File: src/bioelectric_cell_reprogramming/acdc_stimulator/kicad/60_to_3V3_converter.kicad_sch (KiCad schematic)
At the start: 7 parts, among them IC6 LTC3637IMSE#PBF

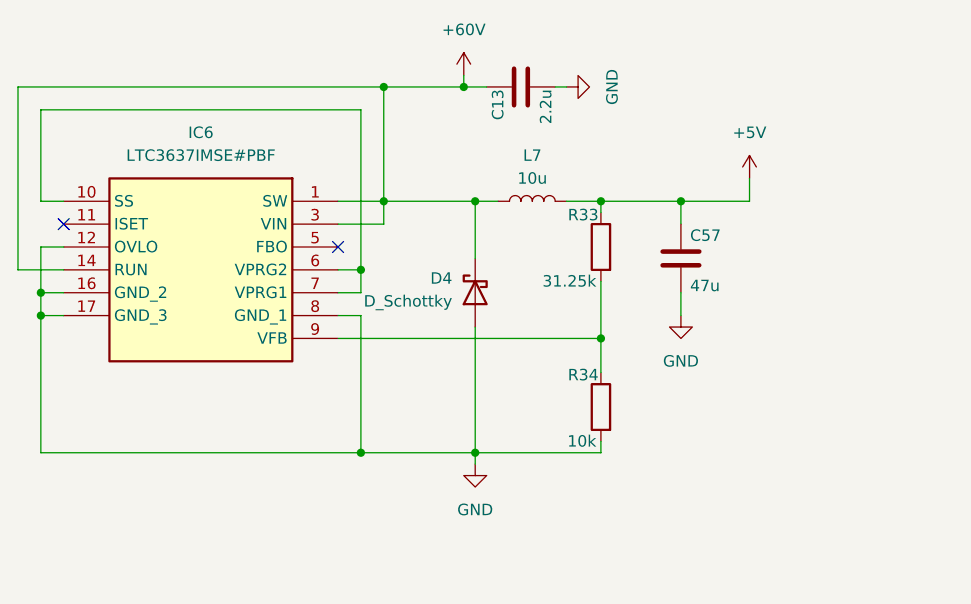
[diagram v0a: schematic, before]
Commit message: CI: footprint assignment done
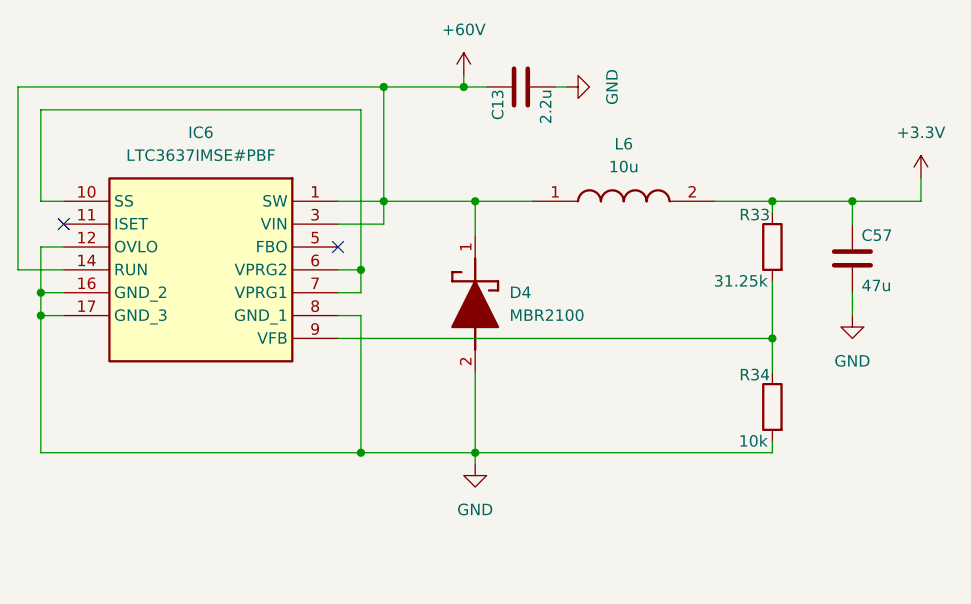
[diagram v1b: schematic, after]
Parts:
- removed D4: D_Schottky, symbol Device:D_Schottky
- removed L7: 10u, symbol Device:L
- added D4: MBR2100, MBR2100:DIOAD1910W86L670D310, symbol MBR2100:MBR2100
- added L6: 10u, SRP1270-100M:INDPM137137X700N, symbol SRP1270-100M:SRP1270-100M
- C13: footprint (none) -> Capacitor_SMD:C_0603_1608Metric
- C57: footprint (none) -> Capacitor_SMD:C_0805_2012Metric
- IC6: footprint LTC3637IMSEPBF -> LTC3637IMSE#PBF:LTC3637IMSEPBF
- R33, R34: footprint (none) -> Resistor_SMD:R_0402_1005Metric
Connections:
- net +60V: now also D4.1 (K), L6.1
- net GND: now also D4.2 (A)
- net +5V renamed +3.3V
- net +3.3V: now also L6.2
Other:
- moved on the sheet: C57, R33, R34

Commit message: ci: STM32 layout done and schematic annotated
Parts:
- renumbered C13 to C57, C57 to C58, L6 to L7, R33 to R32, R34 to R33
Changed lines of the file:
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@@
 		(on_board yes)
 		(dnp no)
-		(property "Reference" "L6"
+		(property "Reference" "L7"
 			(at 172.72 76.2 0)
 			(effects
@@
 			(project ""
 				(path "/ec70e9f6-566f-44ea-8141-5580f51beca4/e479d02d-ff3f-46f9-af62-0bc7155bcaaf"
-					(reference "L6")
+					(reference "L7")
 					(unit 1)
 				)
@@
 		(dnp no)
 		(fields_autoplaced yes)
-		(property "Reference" "#PWR092"
+		(property "Reference" "#PWR097"
 			(at 198.12 101.6 0)
 			(effects
@@
 			(project "acdc_stimulator"
 				(path "/ec70e9f6-566f-44ea-8141-5580f51beca4/e479d02d-ff3f-46f9-af62-0bc7155bcaaf"
-					(reference "#PWR092")
+					(reference "#PWR097")
 					(unit 1)
 				)
@@
 		(dnp no)
 		(fields_autoplaced yes)
-		(property "Reference" "#PWR093"
+		(property "Reference" "#PWR098"
 			(at 205.74 83.82 0)
 			(effects
@@
 			(project "acdc_stimulator"
 				(path "/ec70e9f6-566f-44ea-8141-5580f51beca4/e479d02d-ff3f-46f9-af62-0bc7155bcaaf"
-					(reference "#PWR093")
+					(reference "#PWR098")
 					(unit 1)
 				)
@@
 		(on_board yes)
 		(dnp no)
-		(property "Reference" "C57"
+		(property "Reference" "C58"
 			(at 199.136 86.36 0)
 			(effects
@@
 			(project "acdc_stimulator"
 				(path "/ec70e9f6-566f-44ea-8141-5580f51beca4/e479d02d-ff3f-46f9-af62-0bc7155bcaaf"
-					(reference "C57")
+					(reference "C58")
 					(unit 1)
 				)
@@
 		(on_board yes)
 		(dnp no)
-		(property "Reference" "C13"
+		(property "Reference" "C57"
 			(at 158.75 70.104 0)
 			(effects
@@
 			(project "acdc_stimulator"
 				(path "/ec70e9f6-566f-44ea-8141-5580f51beca4/e479d02d-ff3f-46f9-af62-0bc7155bcaaf"
-					(reference "C13")
+					(reference "C57")
 					(unit 1)
 				)
@@
 		(on_board yes)
 		(dnp no)
-		(property "Reference" "R33"
+		(property "Reference" "R32"
 			(at 188.976 84.074 0)
 			(effects
@@
 			(project "acdc_stimulator"
 				(path "/ec70e9f6-566f-44ea-8141-5580f51beca4/e479d02d-ff3f-46f9-af62-0bc7155bcaaf"
-					(reference "R33")
+					(reference "R32")
 					(unit 1)
 				)
@@
 		(dnp no)
 		(fields_autoplaced yes)
-		(property "Reference" "#PWR090"
+		(property "Reference" "#PWR095"
 			(at 156.21 118.11 0)
 			(effects
@@
 			(project "acdc_stimulator"
 				(path "/ec70e9f6-566f-44ea-8141-5580f51beca4/e479d02d-ff3f-46f9-af62-0bc7155bcaaf"
-					(reference "#PWR090")
+					(reference "#PWR095")
 					(unit 1)
 				)
@@
 		(dnp no)
 		(fields_autoplaced yes)
-		(property "Reference" "#PWR091"
+		(property "Reference" "#PWR096"
 			(at 172.72 69.85 0)
 			(effects
@@
 			(project "acdc_stimulator"
 				(path "/ec70e9f6-566f-44ea-8141-5580f51beca4/e479d02d-ff3f-46f9-af62-0bc7155bcaaf"
-					(reference "#PWR091")
+					(reference "#PWR096")
 					(unit 1)
 				)
@@
 		(dnp no)
 		(fields_autoplaced yes)
-		(property "Reference" "#PWR089"
+		(property "Reference" "#PWR094"
 			(at 154.94 72.39 0)
 			(effects
@@
 			(project "acdc_stimulator"
 				(path "/ec70e9f6-566f-44ea-8141-5580f51beca4/e479d02d-ff3f-46f9-af62-0bc7155bcaaf"
-					(reference "#PWR089")
+					(reference "#PWR094")
 					(unit 1)
 				)
@@
 		(on_board yes)
 		(dnp no)
-		(property "Reference" "R34"
+		(property "Reference" "R33"
 			(at 188.976 101.854 0)
 			(effects
@@
 			(project "acdc_stimulator"
 				(path "/ec70e9f6-566f-44ea-8141-5580f51beca4/e479d02d-ff3f-46f9-af62-0bc7155bcaaf"
-					(reference "R34")
-					(unit 1)
-				)
+					(reference "R33")
+					(unit 1)
+				)

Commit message: ci: layout done
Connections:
- net +60V: no longer D4.1 (K), IC6.1 (SW), L7.1
- new net: D4.1 (K), IC6.1 (SW), L7.1
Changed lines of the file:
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@@
 	(paper "A4")
 	(junction
-		(at 146.05 82.55)
-		(diameter 0)
-		(color 0 0 0 0)
-	)
-	(junction
 		(at 143.51 90.17)
 		(diameter 0)
@@
 	)
 	(junction
+		(at 189.23 82.55)
+		(diameter 0)
+		(color 0 0 0 0)
+	)
+	(junction
+		(at 156.21 82.55)
+		(diameter 0)
+		(color 0 0 0 0)
+	)
+	(junction
 		(at 146.05 69.85)
-		(diameter 0)
-		(color 0 0 0 0)
-	)
-	(junction
-		(at 189.23 82.55)
-		(diameter 0)
-		(color 0 0 0 0)
-	)
-	(junction
-		(at 156.21 82.55)
 		(diameter 0)
 		(color 0 0 0 0)
@@
 	(wire
 		(pts
-			(xy 146.05 82.55) (xy 140.97 82.55)
+			(xy 140.97 82.55) (xy 156.21 82.55)
 		)
 		(stroke
@@
 	(wire
 		(pts
-			(xy 146.05 82.55) (xy 156.21 82.55)
-		)
-		(stroke
-			(width 0)
-			(type default)
-		)
-	)
-	(wire
-		(pts
-			(xy 146.05 69.85) (xy 146.05 82.55)
-		)
-		(stroke
-			(width 0)
-			(type default)
-		)
-	)
-	(wire
-		(pts
 			(xy 143.51 110.49) (xy 156.21 110.49)
 		)
@@
 	(wire
 		(pts
+			(xy 156.21 110.49) (xy 156.21 111.76)
+		)
+		(stroke
+			(width 0)
+			(type default)
+		)
+	)
+	(wire
+		(pts
+			(xy 165.1 69.85) (xy 166.37 69.85)
+		)
+		(stroke
+			(width 0)
+			(type default)
+		)
+	)
+	(wire
+		(pts
+			(xy 189.23 91.44) (xy 189.23 97.79)
+		)
+		(stroke
+			(width 0)
+			(type default)
+		)
+	)
+	(wire
+		(pts
+			(xy 146.05 69.85) (xy 146.05 85.09)
+		)
+		(stroke
+			(width 0)
+			(type default)
+		)
+	)
+	(wire
+		(pts
+			(xy 110.49 90.17) (xy 105.41 90.17)
+		)
+		(stroke
+			(width 0)
+			(type default)
+		)
+	)
+	(wire
+		(pts
+			(xy 107.95 87.63) (xy 110.49 87.63)
+		)
+		(stroke
+			(width 0)
+			(type default)
+		)
+	)
+	(wire
+		(pts
+			(xy 143.51 110.49) (xy 107.95 110.49)
+		)
+		(stroke
+			(width 0)
+			(type default)
+		)
+	)
+	(wire
+		(pts
+			(xy 157.48 69.85) (xy 154.94 69.85)
+		)
+		(stroke
+			(width 0)
+			(type default)
+		)
+	)
+	(wire
+		(pts
+			(xy 143.51 72.39) (xy 143.51 90.17)
+		)
+		(stroke
+			(width 0)
+			(type default)
+		)
+	)
+	(wire
+		(pts
 			(xy 105.41 69.85) (xy 146.05 69.85)
 		)
@@
 	(wire
 		(pts
-			(xy 156.21 110.49) (xy 156.21 111.76)
-		)
-		(stroke
-			(width 0)
-			(type default)
-		)
-	)
-	(wire
-		(pts
-			(xy 165.1 69.85) (xy 166.37 69.85)
-		)
-		(stroke
-			(width 0)
-			(type default)
-		)
-	)
-	(wire
-		(pts
-			(xy 189.23 91.44) (xy 189.23 97.79)
-		)
-		(stroke
-			(width 0)
-			(type default)
-		)
-	)
-	(wire
-		(pts
-			(xy 110.49 90.17) (xy 105.41 90.17)
-		)
-		(stroke
-			(width 0)
-			(type default)
-		)
-	)
-	(wire
-		(pts
-			(xy 107.95 87.63) (xy 110.49 87.63)
-		)
-		(stroke
-			(width 0)
-			(type default)
-		)
-	)
-	(wire
-		(pts
-			(xy 143.51 110.49) (xy 107.95 110.49)
-		)
-		(stroke
-			(width 0)
-			(type default)
-		)
-	)
-	(wire
-		(pts
-			(xy 157.48 69.85) (xy 154.94 69.85)
-		)
-		(stroke
-			(width 0)
-			(type default)
-		)
-	)
-	(wire
-		(pts
-			(xy 143.51 72.39) (xy 143.51 90.17)
-		)
-		(stroke
-			(width 0)
-			(type default)
-		)
-	)
-	(wire
-		(pts
-			(xy 154.94 69.85) (xy 146.05 69.85)
-		)
-		(stroke
-			(width 0)
-			(type default)
-		)
-	)
-	(wire
-		(pts
 			(xy 205.74 80.01) (xy 205.74 82.55)
 		)
@@
 	(wire
 		(pts
+			(xy 146.05 69.85) (xy 154.94 69.85)
+		)
+		(stroke
+			(width 0)
+			(type default)
+		)
+	)
+	(wire
+		(pts
 			(xy 105.41 90.17) (xy 105.41 69.85)
 		)
 		(stroke
-			(width 0)
-			(type default)
-		)
-	)
-	(wire
-		(pts
-			(xy 146.05 82.55) (xy 146.05 85.09)
-		)
-		(stroke

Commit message: fixed some more clearance errors
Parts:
- R33: Distributor Link (none) -> https://jlcpcb.com/partdetail/259901-NQ02WGJ0103TCE/C270371; Manufacturer (none) -> UNI-ROYAL(Uniroyal Elec); Manufacturer Part Number (none) -> NQ02WGJ0103TCE
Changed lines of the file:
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@@
+			)
+		)
+		(property "Distributor Link" ""
+			(at 162.56 82.55 0)
+			(effects
+				(font
+					(size 1.27 1.27)
+				)
+				(hide yes)
+			)
+		)
+		(property "Manufacturer" ""
+			(at 162.56 82.55 0)
+			(effects
+				(font
+					(size 1.27 1.27)
+				)
+				(hide yes)
+			)
+		)
+		(property "Manufacturer Part Number" ""
+			(at 162.56 82.55 0)
+			(effects
+				(font
+					(size 1.27 1.27)
+				)
+				(hide yes)
 			)
 		)
@@
 			)
 		)
+		(property "Distributor Link" ""
+			(at 198.12 88.9 0)
+			(effects
+				(font
+					(size 1.27 1.27)
+				)
+				(hide yes)
+			)
+		)
+		(property "Manufacturer" ""
+			(at 198.12 88.9 0)
+			(effects
+				(font
+					(size 1.27 1.27)
+				)
+				(hide yes)
+			)
+		)
+		(property "Manufacturer Part Number" ""
+			(at 198.12 88.9 0)
+			(effects
+				(font
+					(size 1.27 1.27)
+				)
+				(hide yes)
+			)
+		)
 		(pin "2"
 		)
@@
 			)
 		)
+		(property "Distributor Link" ""
+			(at 161.29 69.85 0)
+			(effects
+				(font
+					(size 1.27 1.27)
+				)
+				(hide yes)
+			)
+		)
+		(property "Manufacturer" ""
+			(at 161.29 69.85 0)
+			(effects
+				(font
+					(size 1.27 1.27)
+				)
+				(hide yes)
+			)
+		)
+		(property "Manufacturer Part Number" ""
+			(at 161.29 69.85 0)
+			(effects
+				(font
+					(size 1.27 1.27)
+				)
+				(hide yes)
+			)
+		)
 		(pin "1"
 		)
@@
 			)
 		)
+		(property "Distributor Link" ""
+			(at 156.21 83.82 0)
+			(effects
+				(font
+					(size 1.27 1.27)
+				)
+				(hide yes)
+			)
+		)
+		(property "Manufacturer" ""
+			(at 156.21 83.82 0)
+			(effects
+				(font
+					(size 1.27 1.27)
+				)
+				(hide yes)
+			)
+		)
+		(property "Manufacturer Part Number" ""
+			(at 156.21 83.82 0)
+			(effects
+				(font
+					(size 1.27 1.27)
+				)
+				(hide yes)
+			)
+		)
 		(pin "1"
 		)
@@
 		)
 		(property "Description" "Resistor"
+			(at 189.23 87.63 0)
+			(effects
+				(font
+					(size 1.27 1.27)
+				)
+				(hide yes)
+			)
+		)
+		(property "Distributor Link" ""
+			(at 189.23 87.63 0)
+			(effects
+				(font
+					(size 1.27 1.27)
+				)
+				(hide yes)
+			)
+		)
+		(property "Manufacturer" ""
+			(at 189.23 87.63 0)
+			(effects
+				(font
+					(size 1.27 1.27)
+				)
+				(hide yes)
+			)
+		)
+		(property "Manufacturer Part Number" ""
 			(at 189.23 87.63 0)
 			(effects
@@
 			)
 		)
+		(property "Distributor Link" "https://jlcpcb.com/partdetail/259901-NQ02WGJ0103TCE/C270371"
+			(at 189.23 105.41 0)
+			(effects
+				(font
+					(size 1.27 1.27)
+				)
+				(hide yes)
+			)
+		)
+		(property "Manufacturer" "UNI-ROYAL(Uniroyal Elec)"
+			(at 189.23 105.41 0)
+			(effects
+				(font
+					(size 1.27 1.27)
+				)
+				(hide yes)
+			)
+		)
+		(property "Manufacturer Part Number" "NQ02WGJ0103TCE"
+			(at 189.23 105.41 0)
+			(effects
+				(font
+					(size 1.27 1.27)
+				)
+				(hide yes)
+			)
+		)
 		(pin "1"
 		)
@@
 				(hide yes)
 			)
+		)
+		(property "Distributor Link" ""
+			(at 140.97 82.55 0)
+			(effects
+				(font
+					(size 1.27 1.27)
+				)
+				(hide yes)
+			)
+		)
+		(property "Manufacturer" ""
+			(at 140.97 82.55 0)
+			(effects
+				(font
+					(size 1.27 1.27)
+				)
+				(hide yes)
+			)
+		)
+		(property "Manufacturer Part Number" ""
+			(at 140.97 82.55 0)
+			(effects
+				(font
+					(size 1.27 1.27)
+				)
+				(hide yes)
+			)

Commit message: BOM in progress
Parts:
- C57: Distributor Link (none) -> https://jlcpcb.com/partdetail/3409988-GRM21BD72A225KE01L/C2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; Manufacturer (none) -> Murata Electronics; Manufacturer Part Number (none) -> GRM21BD72A225KE01L
- C58: footprint Capacitor_SMD:C_0805_2012Metric -> Capacitor_SMD:C_1206_3216Metric; Distributor Link (none) -> https://jlcpcb.com/partdetail/183737-1206X476M160NT/C172351; Manufacturer (none) -> FH (Guangdong Fenghua Advanced Tech); Manufacturer Part Number (none) -> 1206X476M160NT
- D4: Distributor Link (none) -> https://www.digikey.com/en/products/detail/panjit-internati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; Manufacturer (none) -> Panjit International Inc.; Manufacturer Part Number (none) -> MBR2100_R2_00001
- IC6: Distributor Link (none) -> https://jlcpcb.com/partdetail/AnalogDevices-LTC3637IMSEPBF/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; Manufacturer (none) -> Analog Devices; Manufacturer Part Number (none) -> LTC3637IMSE#PBF
- L7: Distributor Link (none) -> https://www.mouser.com/ProductDetail/Bourns/SRP1270-100M?qs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; Manufacturer (none) -> Bourns; Manufacturer Part Number (none) -> SRP1270-100M
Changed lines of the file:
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@@
 			)
 		)
-		(property "Distributor Link" ""
+		(property "Distributor Link" "https://www.mouser.com/ProductDetail/Bourns/SRP1270-100M?qs=s%252BX%2FYkvGCpE5rFNaoMUDIw%3D%3D"
 			(at 162.56 82.55 0)
 			(effects
@@
 			)
 		)
-		(property "Manufacturer" ""
+		(property "Manufacturer" "Bourns"
 			(at 162.56 82.55 0)
 			(effects
@@
 			)
 		)
-		(property "Manufacturer Part Number" ""
+		(property "Manufacturer Part Number" "SRP1270-100M"
+			(at 162.56 82.55 0)
+			(effects
+				(font
+					(size 1.27 1.27)
+				)
+				(hide yes)
+			)
+		)
+		(property "JLCPCB Part #" ""
 			(at 162.56 82.55 0)
 			(effects
@@
 			)
 		)
-		(property "Footprint" "Capacitor_SMD:C_0805_2012Metric"
+		(property "Footprint" "Capacitor_SMD:C_1206_3216Metric"
 			(at 199.0852 92.71 0)
 			(effects
@@
 			)
 		)
-		(property "Distributor Link" ""
+		(property "Distributor Link" "https://jlcpcb.com/partdetail/183737-1206X476M160NT/C172351"
 			(at 198.12 88.9 0)
 			(effects
@@
 			)
 		)
-		(property "Manufacturer" ""
+		(property "Manufacturer" "FH (Guangdong Fenghua Advanced Tech)"
 			(at 198.12 88.9 0)
 			(effects
@@
 			)
 		)
-		(property "Manufacturer Part Number" ""
+		(property "Manufacturer Part Number" "1206X476M160NT"
+			(at 198.12 88.9 0)
+			(effects
+				(font
+					(size 1.27 1.27)
+				)
+				(hide yes)
+			)
+		)
+		(property "JLCPCB Part #" ""
 			(at 198.12 88.9 0)
 			(effects
@@
 			)
 		)
-		(property "Distributor Link" ""
+		(property "Distributor Link" "https://jlcpcb.com/partdetail/3409988-GRM21BD72A225KE01L/C2981733"
 			(at 161.29 69.85 0)
 			(effects
@@
 			)
 		)
-		(property "Manufacturer" ""
+		(property "Manufacturer" " Murata Electronics"
 			(at 161.29 69.85 0)
 			(effects
@@
 			)
 		)
-		(property "Manufacturer Part Number" ""
+		(property "Manufacturer Part Number" "GRM21BD72A225KE01L"
+			(at 161.29 69.85 0)
+			(effects
+				(font
+					(size 1.27 1.27)
+				)
+				(hide yes)
+			)
+		)
+		(property "JLCPCB Part #" ""
 			(at 161.29 69.85 0)
 			(effects
@@
 			)
 		)
-		(property "Distributor Link" ""
+		(property "Distributor Link" "https://www.digikey.com/en/products/detail/panjit-international-inc/MBR2100-R2-00001/15801106"
 			(at 156.21 83.82 0)
 			(effects
@@
 			)
 		)
-		(property "Manufacturer" ""
+		(property "Manufacturer" "Panjit International Inc."
 			(at 156.21 83.82 0)
 			(effects
@@
 			)
 		)
-		(property "Manufacturer Part Number" ""
+		(property "Manufacturer Part Number" "MBR2100_R2_00001"
+			(at 156.21 83.82 0)
+			(effects
+				(font
+					(size 1.27 1.27)
+				)
+				(hide yes)
+			)
+		)
+		(property "JLCPCB Part #" ""
 			(at 156.21 83.82 0)
 			(effects
@@
 		)
 		(property "Manufacturer Part Number" ""
+			(at 189.23 87.63 0)
+			(effects
+				(font
+					(size 1.27 1.27)
+				)
+				(hide yes)
+			)
+		)
+		(property "JLCPCB Part #" ""
 			(at 189.23 87.63 0)
 			(effects
@@
 			)
 		)
+		(property "JLCPCB Part #" ""
+			(at 189.23 105.41 0)
+			(effects
+				(font
+					(size 1.27 1.27)
+				)
+				(hide yes)
+			)
+		)
 		(pin "1"
 		)
@@
 			)
 		)
-		(property "Distributor Link" ""
+		(property "Distributor Link" "https://jlcpcb.com/partdetail/AnalogDevices-LTC3637IMSEPBF/C580783"
 			(at 140.97 82.55 0)
 			(effects
@@
 			)
 		)
-		(property "Manufacturer" ""
+		(property "Manufacturer" "Analog Devices"
 			(at 140.97 82.55 0)
 			(effects
@@
 			)
 		)
-		(property "Manufacturer Part Number" ""
+		(property "Manufacturer Part Number" "LTC3637IMSE#PBF"
 			(at 140.97 82.55 0)
 			(effects
+				(font
+					(size 1.27 1.27)
+				)
+				(hide yes)
+			)
+		)
+		(property "JLCPCB Part #" ""
+			(at 140.97 82.55 0)
+			(effects

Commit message: fixed values for resistive divider of LDOs
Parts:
- L7: Distributor Link https://www.mouser.com/ProductDetail/Bourns/SRP1270-100M?qs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 -> https://jlcpcb.com/partdetail/Bourns-SRP1270100M/C2042024; Manufacturer Bourns -> BOURNS
- R32: value 31.25k -> 8.2k
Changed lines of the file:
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@@
 			)
 		)
-		(property "Distributor Link" "https://www.mouser.com/ProductDetail/Bourns/SRP1270-100M?qs=s%252BX%2FYkvGCpE5rFNaoMUDIw%3D%3D"
+		(property "Distributor Link" "https://jlcpcb.com/partdetail/Bourns-SRP1270100M/C2042024"
 			(at 162.56 82.55 0)
 			(effects
@@
 			)
 		)
-		(property "Manufacturer" "Bourns"
+		(property "Manufacturer" "BOURNS"
 			(at 162.56 82.55 0)
 			(effects
@@
 			)
 		)
-		(property "Value" "31.25k"
+		(property "Value" "8.2k"
 			(at 188.722 91.44 0)
 			(effects

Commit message: ci: BOM done
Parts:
- R32: Distributor Link (none) -> https://jlcpcb.com/partdetail/Koa_SpeerElec-RK73B1ETTP822J/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; Manufacturer (none) -> KOA Speer Elec; Manufacturer Part Number (none) -> RK73B1ETTP822J
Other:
- note added: "VFB (internal feedback voltage) is 1.8V when both Vprg are tied to SS"
- note added: "Vout = 1.8(1+R1/R2)"
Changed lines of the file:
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@@
+		)
+	)
+	(text "VFB (internal feedback voltage) is 1.8V when both Vprg are tied to SS\n"
+		(exclude_from_sim no)
+		(at 157.226 124.206 0)
+		(effects
+			(font
+				(size 1.27 1.27)
+			)
+		)
+	)
+	(text "Vout = 1.8(1+R1/R2)"
+		(exclude_from_sim no)
+		(at 177.8 99.568 0)
+		(effects
+			(font
+				(size 1.27 1.27)
+			)
 		)
 	)
@@
 			)
 		)
-		(property "Distributor Link" ""
+		(property "Distributor Link" "https://jlcpcb.com/partdetail/Koa_SpeerElec-RK73B1ETTP822J/C131629"
 			(at 189.23 87.63 0)
 			(effects
@@
 			)
 		)
-		(property "Manufacturer" ""
+		(property "Manufacturer" "KOA Speer Elec"
 			(at 189.23 87.63 0)
 			(effects
@@
 			)
 		)
-		(property "Manufacturer Part Number" ""
+		(property "Manufacturer Part Number" "RK73B1ETTP822J"
 			(at 189.23 87.63 0)
 			(effects

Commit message: ci: build files for v0.0.2 generated
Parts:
- removed D4: MBR2100, MBR2100:DIOAD1910W86L670D310, symbol MBR2100:MBR2100
- removed L7: 10u, SRP1270-100M:INDPM137137X700N, symbol SRP1270-100M:SRP1270-100M
- added D3: B2100AE-13, DIOM5226X240N, symbol B2100AE-13:B2100AE-13
- added L6: 10u, INDPM8080X420N, symbol SWPA8040S100MT:SWPA8040S100MT
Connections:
- net +3.3V: now also L6.2
- net GND: now also D3.2 (A)
- net at IC6.1 (SW): now also D3.1 (K), L6.1
